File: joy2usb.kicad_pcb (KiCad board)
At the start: 2 copper layers, 55 x 90 mm, 18 parts, among them J1 DB9_Male, J2 Conn_02x04_Odd_Even, SW1 RST, SW2 SW_SPDT, U1 Arduino_Pro_Micro, U2 4066

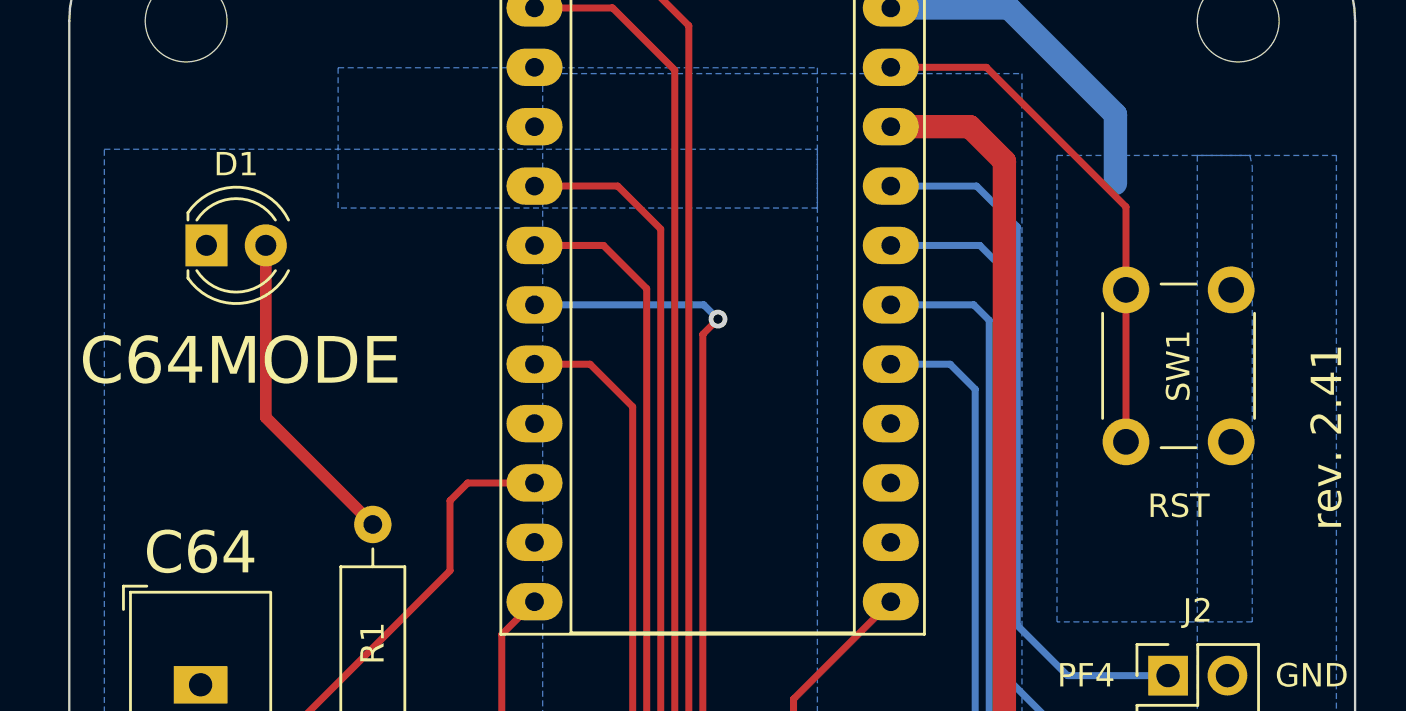
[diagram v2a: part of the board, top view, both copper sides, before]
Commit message: PCB Rev. 2.5
Update of LED footprint
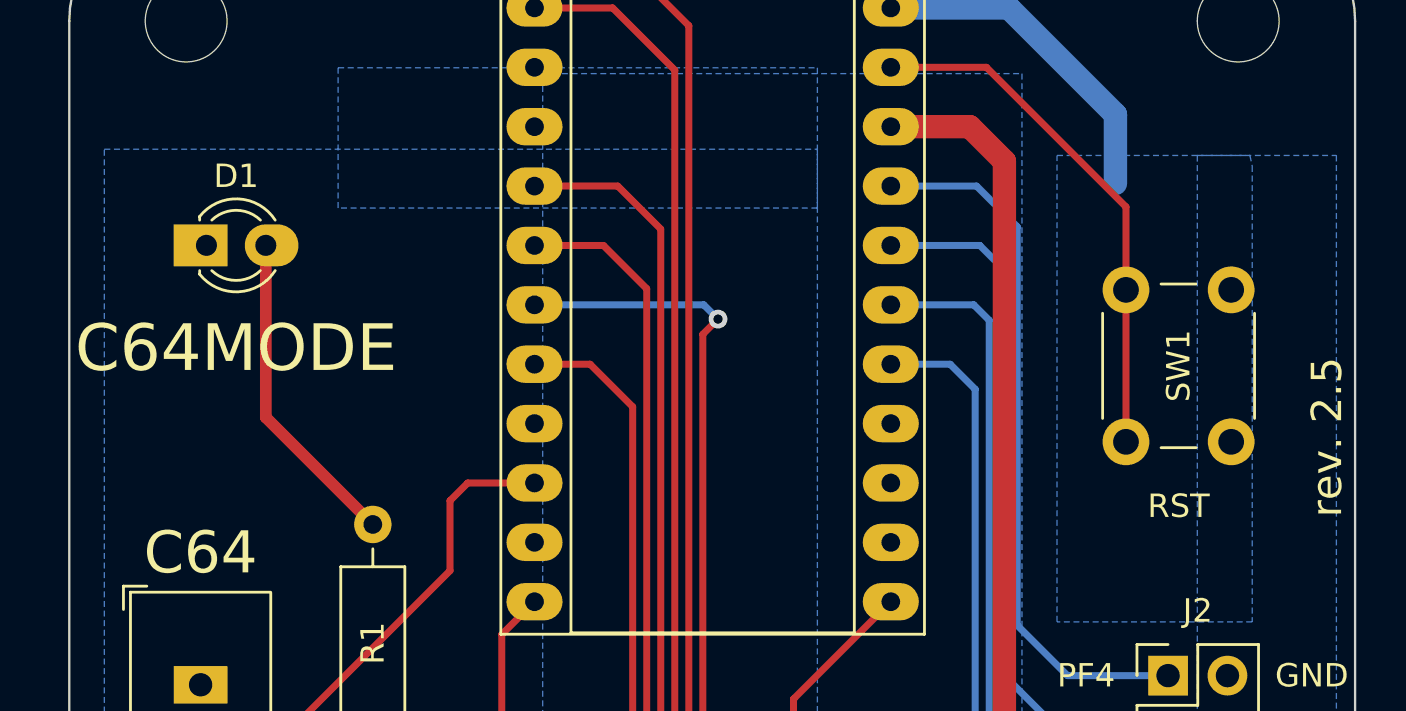
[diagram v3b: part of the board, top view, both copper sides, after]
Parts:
- D1: footprint LED_THT:LED_D4.0mm -> Misc:LED_D3.0mm_Oval
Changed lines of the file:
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@@
   (title_block
     (title "joy2usb")
-    (rev "2.41")
+    (rev "2.5")
     (company "mistepien")
   )
@@
     (pad "" np_thru_hole circle (at 0 0) (size 3.5 3.5) (drill 3.5) (layers *.Cu *.Mask))
   )
-  (footprint "LED_THT:LED_D4.0mm" (layer "F.Cu")
+  (footprint "Misc:LED_D3.0mm_Oval" (layer "F.Cu")
     (at 118.867 69.596)
-    (descr "LED, diameter 4.0mm, 2 pins, http://www.kingbright.com/attachments/file/psearch/000/00/00/L-43GD(Ver.12B).pdf")
-    (tags "LED diameter 4.0mm 2 pins")
+    (descr "LED, diameter 3.0mm, 2 pins")
+    (tags "LED diameter 3.0mm 2 pins")
     (property "Sheetfile" "File: joy2usb.kicad_sch")
     (property "Sheetname" "")
     (attr through_hole)
-    (fp_text reference "D1" (at 1.27 -3.46) (layer "F.SilkS")
-      (effects (font (size 1 1) (thickness 0.15)))
-    )
-    (fp_text value "C64MODE" (at 1.453519 4.95) (layer "F.SilkS")
-      (effects (font (size 2 2) (thickness 0.3)))
-    )
-    (fp_line (start -0.79 -1.399) (end -0.79 -1.08) (layer "F.SilkS") (width 0.12))
-    (fp_line (start -0.79 1.08) (end -0.79 1.399) (layer "F.SilkS") (width 0.12))
-    (fp_arc (start 2.952713 1.080961) (mid 1.269429 2) (end -0.41333 1.08) (layer "F.SilkS") (width 0.12))
-    (fp_arc (start 3.513242 1.080724) (mid 1.453519 2.483228) (end -0.79 1.398749) (layer "F.SilkS") (width 0.12))
-    (fp_arc (start -0.41333 -1.08) (mid 1.269429 -2) (end 2.952713 -1.080961) (layer "F.SilkS") (width 0.12))
-    (fp_arc (start -0.79 -1.398749) (mid 1.453519 -2.483228) (end 3.513242 -1.080724) (layer "F.SilkS") (width 0.12))
-    (fp_line (start -1.45 -2.75) (end -1.45 2.75) (layer "F.CrtYd") (width 0.05))
-    (fp_line (start 4 2.75) (end 4 -2.75) (layer "F.CrtYd") (width 0.05))
-    (fp_line (start -1.45 2.75) (end 4 2.75) (layer "F.CrtYd") (width 0.05))
-    (fp_line (start 4 -2.75) (end -1.45 -2.75) (layer "F.CrtYd") (width 0.05))
-    (fp_line (start -0.73 -1.32665) (end -0.73 1.32665) (layer "F.Fab") (width 0.1))
-    (fp_arc (start -0.73 -1.32665) (mid 3.67 0.000306) (end -0.730339 1.32614) (layer "F.Fab") (width 0.1))
-    (fp_circle (center 1.27 0) (end 3.27 0) (layer "F.Fab") (width 0.1) (fill none))
-    (pad "1" thru_hole rect (at 0 0) (size 1.8 1.8) (drill 0.9) (layers *.Cu *.Mask)
+    (fp_text reference "D1" (at 1.27 -2.96) (layer "F.SilkS")
+      (effects (font (size 1 1) (thickness 0.15)))
+    )
+    (fp_text value "C64MODE" (at 1.270117 4.404) (layer "F.SilkS")
+      (effects (font (size 2 2) (thickness 0.4)))
+    )
+    (fp_line (start -0.29 -1.236) (end -0.29 -1.08) (layer "F.SilkS") (width 0.12))
+    (fp_line (start -0.29 1.08) (end -0.29 1.236) (layer "F.SilkS") (width 0.12))
+    (fp_arc (start 0.229039 -1.08) (mid 1.270117 -1.5) (end 2.31113 -1.079837) (layer "F.SilkS") (width 0.12))
+    (fp_arc (start -0.29 -1.235516) (mid 1.366487 -1.987659) (end 2.942335 -1.078608) (layer "F.SilkS") (width 0.12))
+    (fp_arc (start 2.31113 1.079837) (mid 1.270117 1.5) (end 0.229039 1.08) (layer "F.SilkS") (width 0.12))
+    (fp_arc (start 2.942335 1.078608) (mid 1.366487 1.987659) (end -0.29 1.235516) (layer "F.SilkS") (width 0.12))
+    (fp_line (start 4.25 2.25) (end 4.25 -2.25) (layer "F.CrtYd") (width 0.05))
+    (fp_line (start -1.75 -2.25) (end -1.75 2.25) (layer "F.CrtYd") (width 0.05))
+    (fp_line (start 4.25 -2.25) (end -1.75 -2.25) (layer "F.CrtYd") (width 0.05))
+    (fp_line (start -1.75 2.25) (end 4.25 2.25) (layer "F.CrtYd") (width 0.05))
+    (fp_line (start -0.23 -1.16619) (end -0.23 1.16619) (layer "F.Fab") (width 0.1))
+    (fp_arc (start -0.23 -1.16619) (mid 3.17 0.000452) (end -0.230555 1.165476) (layer "F.Fab") (width 0.1))
+    (fp_circle (center 1.27 0) (end 2.77 0) (layer "F.Fab") (width 0.1) (fill none))
+    (pad "1" thru_hole rect (at 0 0 90) (size 1.8 2.3) (drill 0.9 (offset 0 -0.25)) (layers *.Cu *.Mask)
       (net 8 "GND1") (pinfunction "K") (pintype "passive"))
-    (pad "2" thru_hole circle (at 2.54 0) (size 1.8 1.8) (drill 0.9) (layers *.Cu *.Mask)
+    (pad "2" thru_hole oval (at 2.54 0 90) (size 1.8 2.3) (drill 0.9 (offset 0 0.25)) (layers *.Cu *.Mask)
       (net 21 "Net-(D1-Pad2)") (pinfunction "A") (pintype "passive"))
-    (model "${KICAD6_3DMODEL_DIR}/LED_THT.3dshapes/LED_D4.0mm.wrl"
+    (model "${KICAD6_3DMODEL_DIR}/LED_THT.3dshapes/LED_D3.0mm.wrl"
       (offset (xyz 0 0 0))
       (scale (xyz 1 1 1))
@@
   (segment (start 160 88) (end 155.7 88) (width 0.3) (layer "B.Cu") (net 20))
   (segment (start 153.55 68.8) (end 151.81 67.06) (width 0.3) (layer "B.Cu") (net 20))
+  (segment (start 125.984 81.534) (end 121.407 76.957) (width 0.5) (layer "F.Cu") (net 21))
   (segment (start 121.407 76.957) (end 121.407 69.596) (width 0.5) (layer "F.Cu") (net 21))
-  (segment (start 125.984 81.534) (end 121.407 76.957) (width 0.5) (layer "F.Cu") (net 21))
   (segment (start 118.618 90.932) (end 121.86625 90.932) (width 0.3) (layer "F.Cu") (net 23))
   (segment (start 129.286 83.51225) (end 129.286 80.518) (width 0.3) (layer "F.Cu") (net 23))

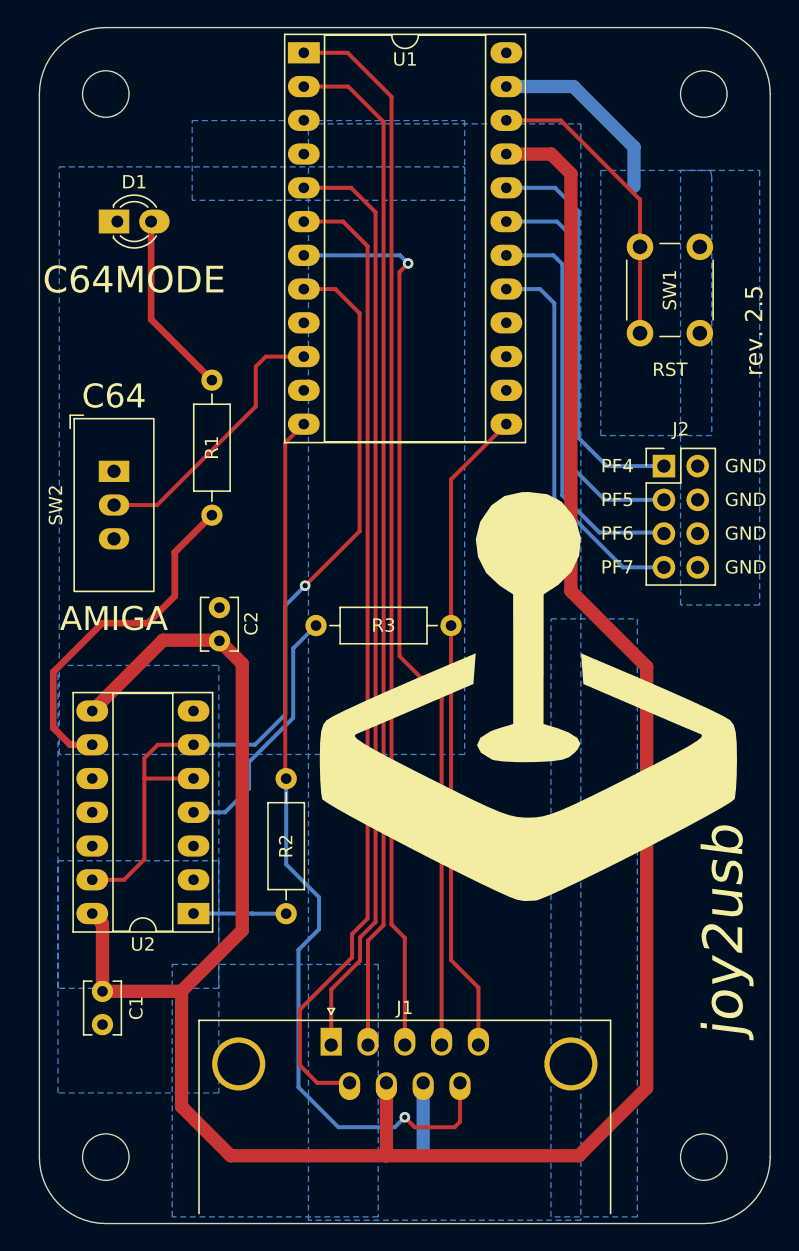
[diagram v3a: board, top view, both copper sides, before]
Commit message: PCB Rev. 3.0
Replace GND1 and GND2 with GND.
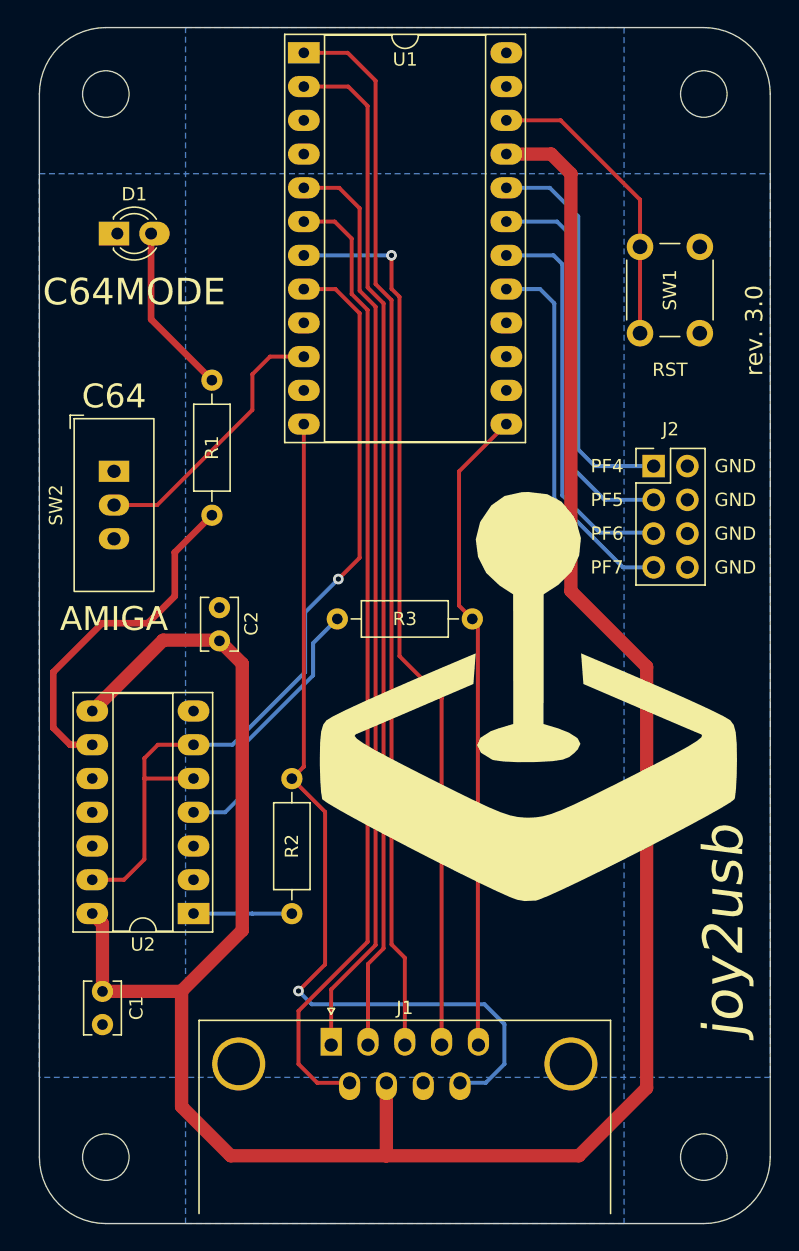
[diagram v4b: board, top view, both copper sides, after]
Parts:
- removed the REF** at (152.5, 112.5)
- added REF**: OSHW-Logo_28.5x30mm_SilkScreen, Symbol:OSHW-Logo_28.5x30mm_SilkScreen, B.Cu at (149.5, 112.5)
- moved R3 1.68 mm to (135.4, 99.5)
- moved D1 0.90 mm to (118.9, 70.5)
- moved J2 0.78 mm to (159.2, 88.0)
- moved R2 0.43 mm to (132.0, 111.5)
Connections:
- C1 pad 2: GND1 -> GND
- C2 pad 2: GND1 -> GND
- D1 pad 1: GND1 -> GND
- J1 pad 8: GND1 -> GND
- J2 pad 2: GND2 -> GND
- J2 pad 4: GND2 -> GND
- J2 pad 6: GND2 -> GND
- J2 pad 8: GND2 -> GND
- SW1 pad 2: GND2 -> GND
- SW2 pad 1: GND1 -> GND
- U1 pad 23: GND2 -> GND
- U1 pad 3: unconnected-(U1-Pad3) -> GND
- U1 pad 4: GND1 -> GND
- U2 pad 10: GND1 -> GND
- U2 pad 11: GND1 -> GND
- U2 pad 12: GND1 -> GND
- U2 pad 2: GND1 -> GND
- U2 pad 3: GND1 -> GND
- U2 pad 7: GND1 -> GND
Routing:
- net GND2: track 14.4 -> 0.00 mm
- net GND1: track 5.28 -> 0.00 mm
- net Net-(R3-Pad1): track 19.3 -> 20.4 mm
- net /F2F3MODE: track 65.3 -> 64.3 mm
- net /RBTN: track 68.5 -> 67.6 mm
- net Net-(D1-Pad2): track 13.8 -> 12.9 mm
- net /F2BTN: track 69.2 -> 68.4 mm
- net /PF7: track 29.1 -> 28.4 mm
- net /PF5: track 30.7 -> 29.9 mm
- net /PF6: track 30.7 -> 30.0 mm
- net /UBTN: track 70.2 -> 69.7 mm
- added copper zone on B.Cu, net GND
- removed copper zone on B.Cu, net GND1
- removed copper zone on B.Cu, net GND2
